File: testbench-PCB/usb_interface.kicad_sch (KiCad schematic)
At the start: 6 parts, among them J1 USB_C_Receptacle_USB2.0, U9 USBLC6-2SC6

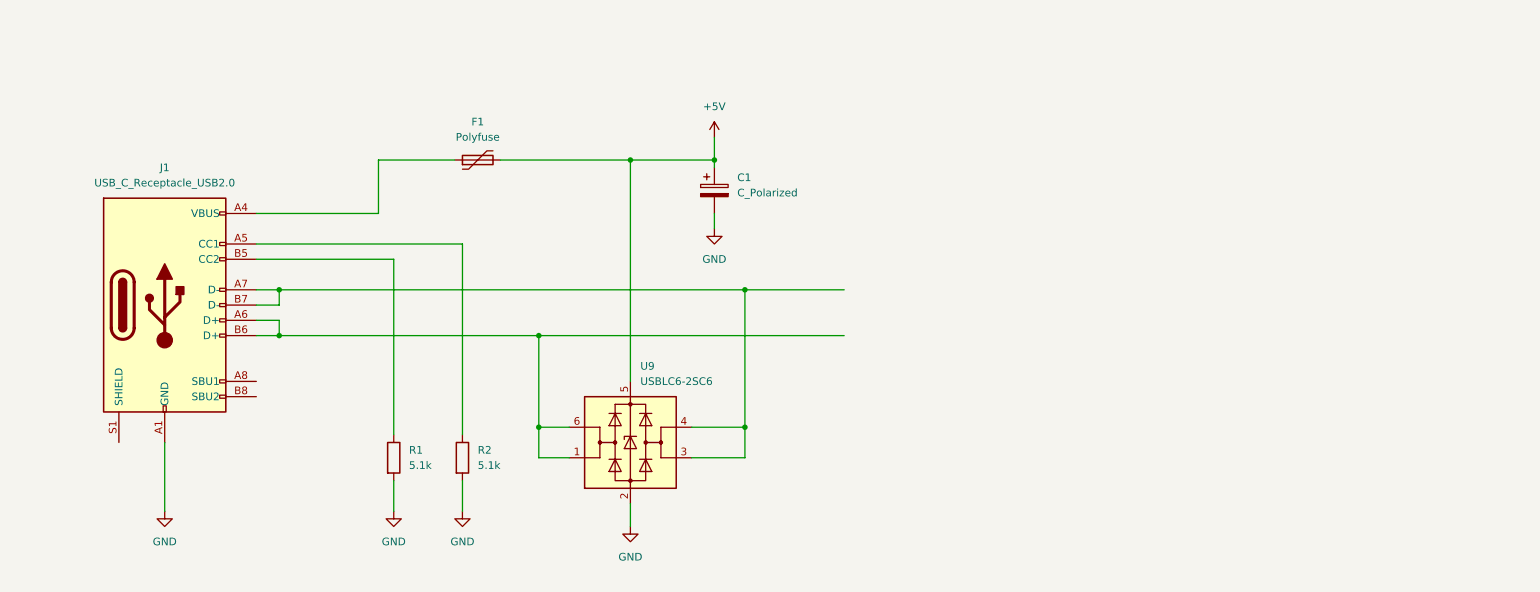
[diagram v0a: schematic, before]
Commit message: Added USB interface.
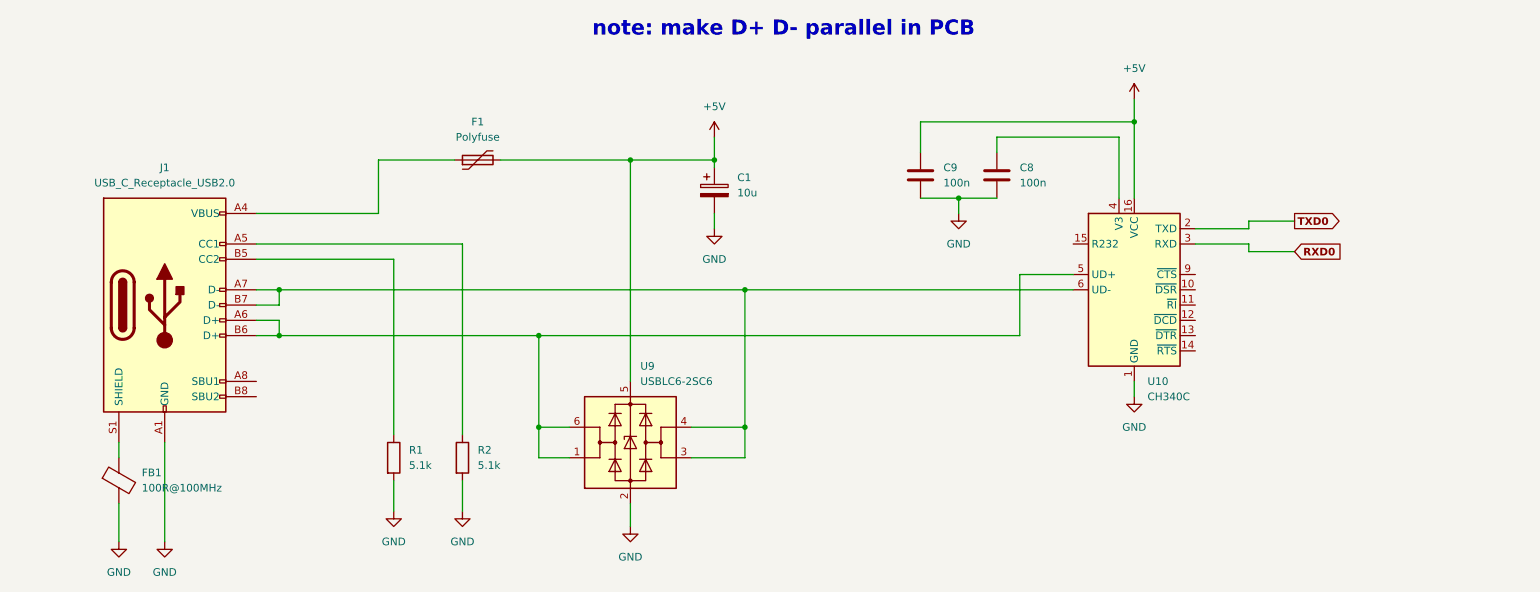
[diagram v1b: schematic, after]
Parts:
- added C8, C9: 100n, Capacitor_SMD:C_0805_2012Metric, symbol Device:C
- added FB1: 100R@100MHz, Inductor_SMD:L_0805_2012Metric, symbol Device:FerriteBead
- added U10: CH340C, Package_SO:SOIC-16_3.9x9.9mm_P1.27mm, symbol Interface_USB:CH340C
- C1: value C_Polarized -> 10u
- R1, R2: footprint (none) -> Resistor_SMD:R_0805_2012Metric
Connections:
- net +5V: now also C9.1, U10.16 (VCC)
- net GND: now also C8.2, C9.2, FB1.2, U10.1 (GND)
- net at J1.A6 (D+), J1.B6 (D+), U9.1 (I/O1)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: now also U10.5 (UD+)
- net at J1.A7 (D-), J1.B7 (D-), U9.3 (I/O2)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: now also U10.6 (UD-)
- net at J1.S1 (SHIELD): now also FB1.1
- new net: C8.1, U10.4 (V3)
- new net RXD0: U10.3 (RXD)
- new net TXD0: U10.2 (TXD)
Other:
- note added: "note: make D+ D- parallel in PCB"

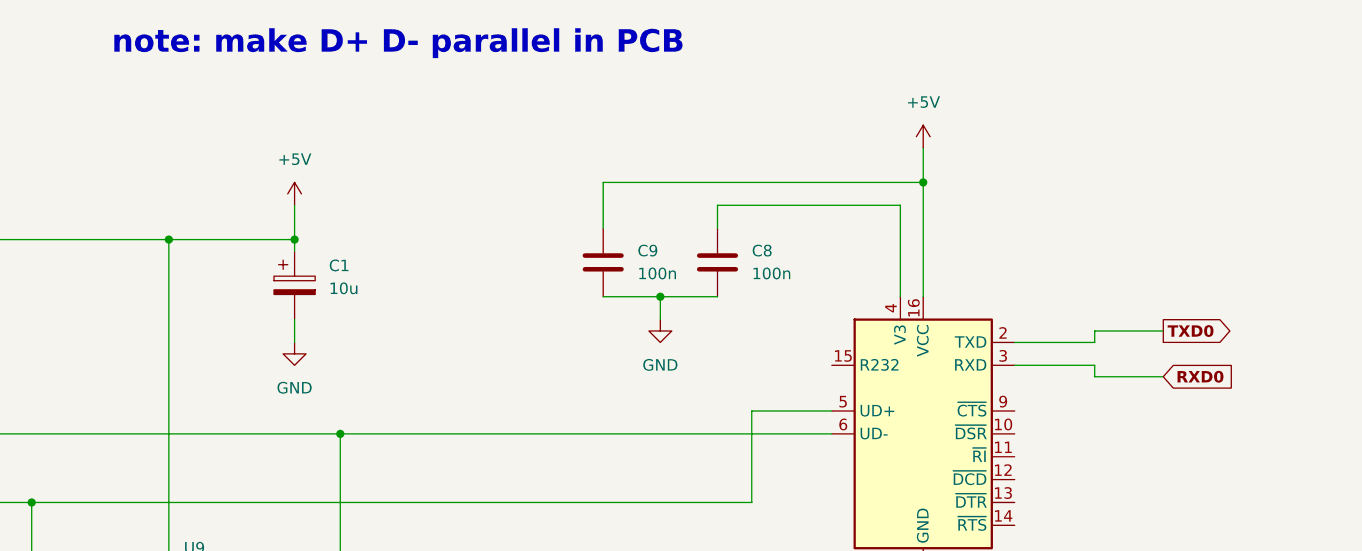
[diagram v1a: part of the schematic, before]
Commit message: Added connection between some modules.
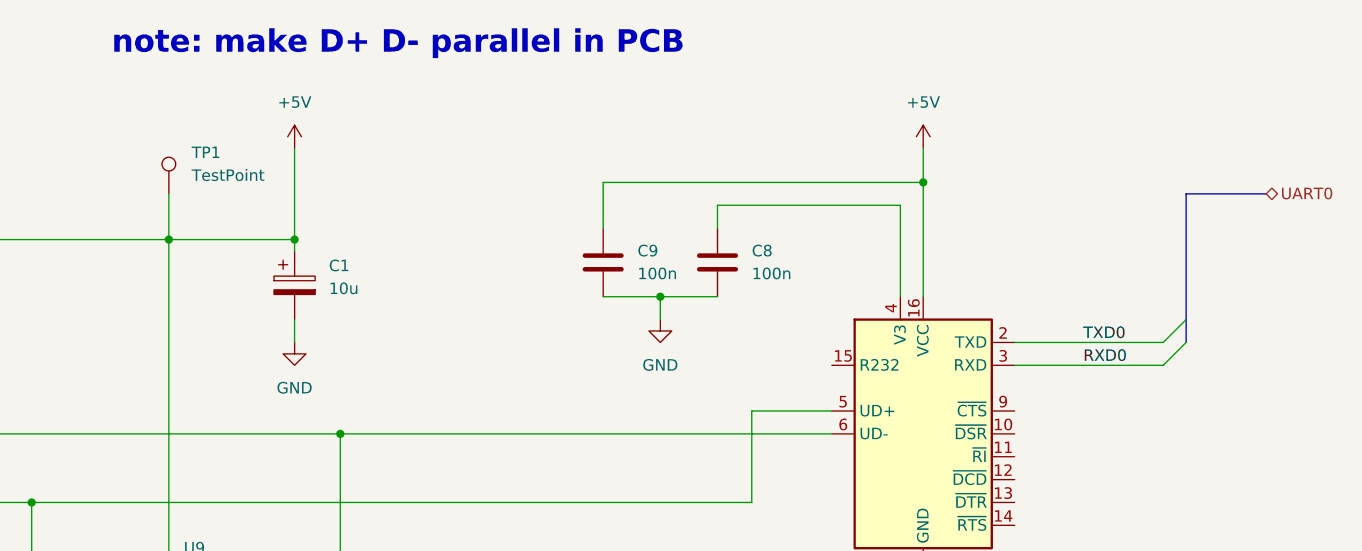
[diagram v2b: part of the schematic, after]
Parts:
- added TP1: TestPoint, TestPoint:TestPoint_Keystone_5005-5009_Compact, symbol Connector:TestPoint
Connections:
- net +5V: now also TP1.1
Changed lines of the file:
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@@
   (junction (at 208.28 50.8) (diameter 0) (color 0 0 0 0)
   )
+  (bus_entry (at 237.49 66.04) (size -2.54 2.54)
+    (stroke (width 0) (type default))
+  )
+  (bus_entry (at 237.49 68.58) (size -2.54 2.54)
+    (stroke (width 0) (type default))
+  )
+  (wire (pts (xy 218.44 71.12) (xy 234.95 71.12))
+    (stroke (width 0) (type default))
+  )
   (wire (pts (xy 62.23 81.28) (xy 66.04 81.28))
     (stroke (width 0) (type default))
@@
     (stroke (width 0) (type default))
   )
-  (wire (pts (xy 227.33 71.12) (xy 218.44 71.12))
+  (bus (pts (xy 237.49 52.07) (xy 237.49 66.04))
     (stroke (width 0) (type default))
   )
@@
     (stroke (width 0) (type default))
   )
-  (wire (pts (xy 227.33 72.39) (xy 227.33 71.12))
-    (stroke (width 0) (type default))
-  )
   (wire (pts (xy 82.55 66.04) (xy 62.23 66.04))
     (stroke (width 0) (type default))
@@
     (stroke (width 0) (type default))
   )
-  (wire (pts (xy 227.33 72.39) (xy 234.95 72.39))
+  (wire (pts (xy 124.46 52.07) (xy 124.46 57.15))
     (stroke (width 0) (type default))
   )
@@
     (stroke (width 0) (type default))
   )
+  (bus (pts (xy 237.49 52.07) (xy 246.38 52.07))
+    (stroke (width 0) (type default))
+  )
+  (bus (pts (xy 237.49 68.58) (xy 237.49 66.04))
+    (stroke (width 0) (type default))
+  )
   (wire (pts (xy 179.07 63.5) (xy 179.07 66.04))
     (stroke (width 0) (type default))
@@
     (stroke (width 0) (type default))
   )
-  (wire (pts (xy 227.33 68.58) (xy 227.33 67.31))
-    (stroke (width 0) (type default))
-  )
   (wire (pts (xy 172.72 63.5) (xy 179.07 63.5))
     (stroke (width 0) (type default))
@@
     (stroke (width 0) (type default))
   )
-  (wire (pts (xy 218.44 68.58) (xy 227.33 68.58))
-    (stroke (width 0) (type default))
-  )
   (wire (pts (xy 66.04 86.36) (xy 62.23 86.36))
     (stroke (width 0) (type default))
@@
     (stroke (width 0) (type default))
   )
+  (wire (pts (xy 218.44 68.58) (xy 234.95 68.58))
+    (stroke (width 0) (type default))
+  )
   (wire (pts (xy 124.46 57.15) (xy 138.43 57.15))
     (stroke (width 0) (type default))
   )
-  (wire (pts (xy 138.43 57.15) (xy 138.43 53.34))
+  (wire (pts (xy 138.43 57.15) (xy 138.43 46.99))
     (stroke (width 0) (type default))
   )
@@
   )
   (wire (pts (xy 208.28 93.98) (xy 208.28 96.52))
-    (stroke (width 0) (type default))
-  )
-  (wire (pts (xy 227.33 67.31) (xy 234.95 67.31))
     (stroke (width 0) (type default))
   )
@@
     (effects (font (size 2.5 2.5) (thickness 0.254) bold (color 255 0 0 1)) (justify left bottom))
   )
-  (global_label "TXD0" (shape output) (at 234.95 67.31 0) (fields_autoplaced)
-    (effects (font (size 1.27 1.27) bold) (justify left))
-    (property "Intersheetrefs" "${INTERSHEET_REFS}" (at 243.0678 67.31 0)
-      (effects (font (size 1.27 1.27)) (justify left) hide)
-    )
-  )
-  (global_label "RXD0" (shape input) (at 234.95 72.39 0) (fields_autoplaced)
-    (effects (font (size 1.27 1.27) bold) (justify left))
-    (property "Intersheetrefs" "${INTERSHEET_REFS}" (at 243.3702 72.39 0)
-      (effects (font (size 1.27 1.27)) (justify left) hide)
-    )
+  (label "TXD0" (at 226.06 68.58 0) (fields_autoplaced)
+    (effects (font (size 1.27 1.27)) (justify left bottom))
+  )
+  (label "RXD0" (at 226.06 71.12 0) (fields_autoplaced)
+    (effects (font (size 1.27 1.27)) (justify left bottom))
+  )
+  (hierarchical_label "UART0" (shape bidirectional) (at 246.38 52.07 0) (fields_autoplaced)
+    (effects (font (size 1.27 1.27)) (justify left))
   )
   (symbol (lib_id "power:GND") (at 179.07 66.04 0) (unit 1)
@@
     )
   )
-  (symbol (lib_id "power:+5V") (at 138.43 53.34 0) (unit 1)
-    (in_bom yes) (on_board yes) (dnp no) (fields_autoplaced)
-    (property "Reference" "#PWR06" (at 138.43 57.15 0)
-      (effects (font (size 1.27 1.27)) hide)
-    )
-    (property "Value" "+5V" (at 138.43 48.26 0)
-      (effects (font (size 1.27 1.27)))
-    )
-    (property "Footprint" "" (at 138.43 53.34 0)
-      (effects (font (size 1.27 1.27)) hide)
-    )
-    (property "Datasheet" "" (at 138.43 53.34 0)
+  (symbol (lib_id "power:+5V") (at 138.43 46.99 0) (unit 1)
+    (in_bom yes) (on_board yes) (dnp no) (fields_autoplaced)
+    (property "Reference" "#PWR06" (at 138.43 50.8 0)
+      (effects (font (size 1.27 1.27)) hide)
+    )
+    (property "Value" "+5V" (at 138.43 41.91 0)
+      (effects (font (size 1.27 1.27)))
+    )
+    (property "Footprint" "" (at 138.43 46.99 0)
+      (effects (font (size 1.27 1.27)) hide)
+    )
+    (property "Datasheet" "" (at 138.43 46.99 0)
       (effects (font (size 1.27 1.27)) hide)
     )
@@
         )
       )
+    )
+  )
+  (symbol (lib_id "Connector:TestPoint") (at 124.46 52.07 0) (unit 1)
+    (in_bom yes) (on_board yes) (dnp no) (fields_autoplaced)
+    (property "Reference" "TP1" (at 127 47.498 0)
+      (effects (font (size 1.27 1.27)) (justify left))
+    )
+    (property "Value" "TestPoint" (at 127 50.038 0)
+      (effects (font (size 1.27 1.27)) (justify left))
+    )
+    (property "Footprint" "TestPoint:TestPoint_Keystone_5005-5009_Compact" (at 129.54 52.07 0)
+      (effects (font (size 1.27 1.27)) hide)
+    )
+    (property "Datasheet" "~" (at 129.54 52.07 0)
+      (effects (font (size 1.27 1.27)) hide)
+    )
+    (pin "1")
+    (instances
+      (project "testbench"
+        (path "/3ac6901d-218d-4b34-8c4a-bf7c417c33bc/85a3a829-d3a3-466d-ad77-bb3f90e9de82"
+          (reference "TP1") (unit 1)
+        )
+      )

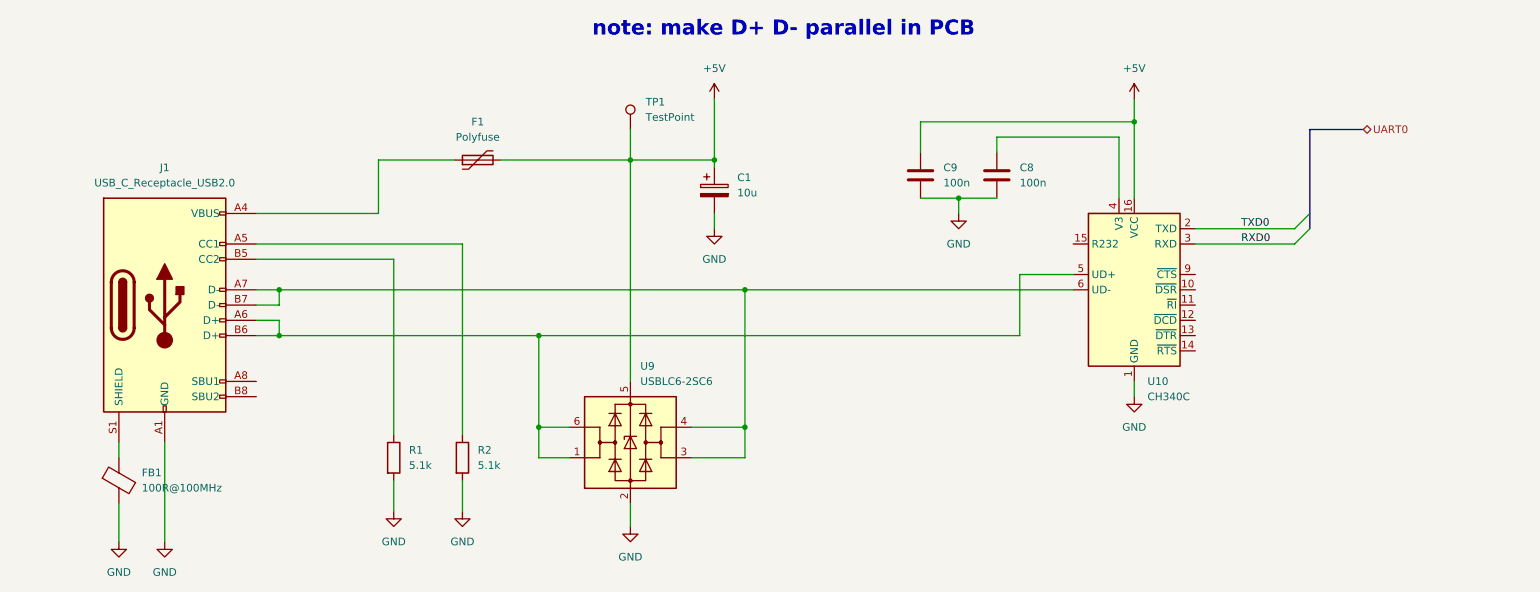
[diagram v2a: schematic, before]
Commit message: Finished connection between modules and MCU.
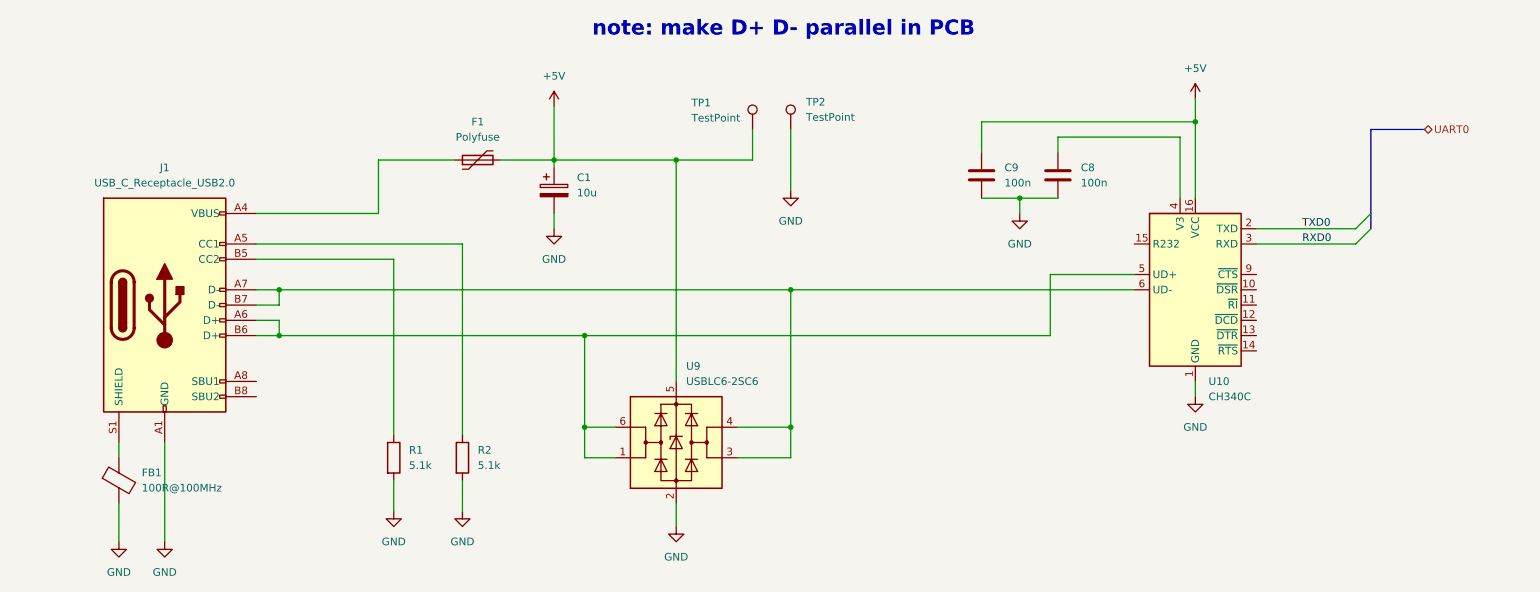
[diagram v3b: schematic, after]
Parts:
- added TP2: TestPoint, TestPoint:TestPoint_Keystone_5005-5009_Compact, symbol Connector:TestPoint
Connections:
- net GND: now also TP2.1
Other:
- moved on the sheet: C1, C8, C9, TP1, U10, U9

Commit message: Changed naming convention.
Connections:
- net RXD0 renamed UART0_RXD
- net TXD0 renamed UART0_TXD
- no-connect marks 0 -> 9
